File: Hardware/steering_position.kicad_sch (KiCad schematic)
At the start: 11 parts, among them U10 MCP6001-OT, U23 MCP6001-OT

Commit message: Changes in power section
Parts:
- TP29, TP30: footprint TestPoint:TestPoint_Pad_D1.0mm -> TestPoint:TestPoint_THTPad_D1.0mm_Drill0.5mm
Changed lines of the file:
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@@
 			)
 		)
-		(property "Footprint" "TestPoint:TestPoint_Pad_D1.0mm"
+		(property "Footprint" "TestPoint:TestPoint_THTPad_D1.0mm_Drill0.5mm"
 			(at 163.83 83.82 0)
 			(effects
@@
 			)
 		)
-		(property "Footprint" "TestPoint:TestPoint_Pad_D1.0mm"
+		(property "Footprint" "TestPoint:TestPoint_THTPad_D1.0mm_Drill0.5mm"
 			(at 139.7 81.28 0)
 			(effects

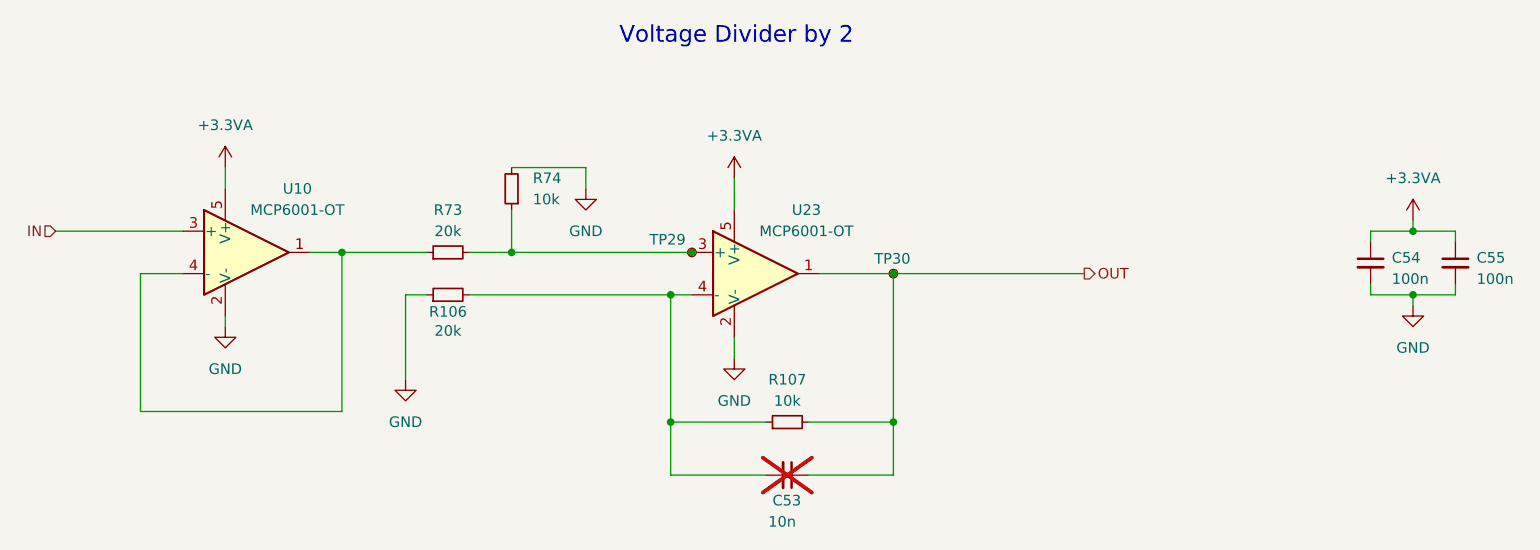
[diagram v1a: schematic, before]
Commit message: Changes Vcc op-amps in brakes pressure (3V3 to 5V) and mcp6002 footprint (to MSOP8)
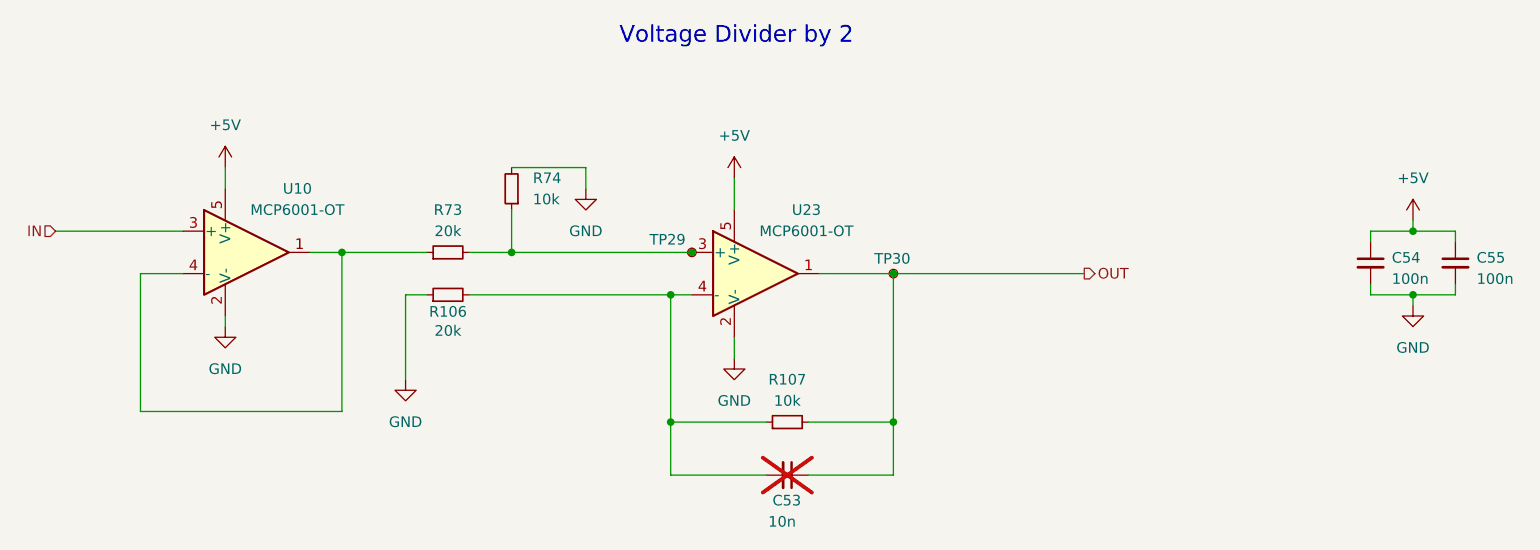
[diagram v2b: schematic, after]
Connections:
- net +3.3VA renamed +5V
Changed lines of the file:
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@@
 	)
 	(symbol
-		(lib_id "power:+3.3VA")
+		(lib_id "power:+5V")
 		(at 78.74 71.12 0)
 		(unit 1)
@@
 			)
 		)
-		(property "Value" "+3.3VA"
+		(property "Value" "+5V"
 			(at 78.74 66.04 0)
 			(effects
@@
 			)
 		)
-		(property "Description" "Power symbol creates a global label with name \"+3.3VA\""
+		(property "Description" "Power symbol creates a global label with name \"+5V\""
 			(at 78.74 71.12 0)
 			(effects
@@
 	)
 	(symbol
-		(lib_id "power:+3.3VA")
+		(lib_id "power:+5V")
 		(at 139.7 72.39 0)
 		(unit 1)
@@
 			)
 		)
-		(property "Value" "+3.3VA"
+		(property "Value" "+5V"
 			(at 139.7 67.31 0)
 			(effects
@@
 			)
 		)
-		(property "Description" "Power symbol creates a global label with name \"+3.3VA\""
+		(property "Description" "Power symbol creates a global label with name \"+5V\""
 			(at 139.7 72.39 0)
 			(effects
@@
 		)
 		(instances
-			(project ""
+			(project "PUTM_EV_Frontbox_2023"
 				(path "/b652b05a-4e3d-4ad1-b032-18886abe7d45/a1f51b52-eb43-44bd-ad58-3192444d1202"
 					(reference "#PWR0154")
@@
 	)
 	(symbol
-		(lib_id "power:+3.3VA")
+		(lib_id "power:+5V")
 		(at 220.98 77.47 0)
 		(unit 1)
@@
 		(on_board yes)
 		(dnp no)
+		(fields_autoplaced yes)
 		(property "Reference" "#PWR0156"
 			(at 220.98 81.28 0)
@@
 			)
 		)
-		(property "Value" "+3.3VA"
+		(property "Value" "+5V"
 			(at 220.98 72.39 0)
 			(effects
@@
 			)
 		)
-		(property "Description" ""
+		(property "Description" "Power symbol creates a global label with name \"+5V\""
 			(at 220.98 77.47 0)
 			(effects
